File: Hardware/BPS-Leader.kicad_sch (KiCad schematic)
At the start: 28 parts, among them J17 Conn_01x04, J21 SFH11-PBPC-D05-ST-BK, J5 Conn_02x06_Counter_Clockwise, J6 PeripheralCAN, J7 PeripheralCAN, J8 CarCANConnector, Q11 PMV213SN,215, U12 SHT4x

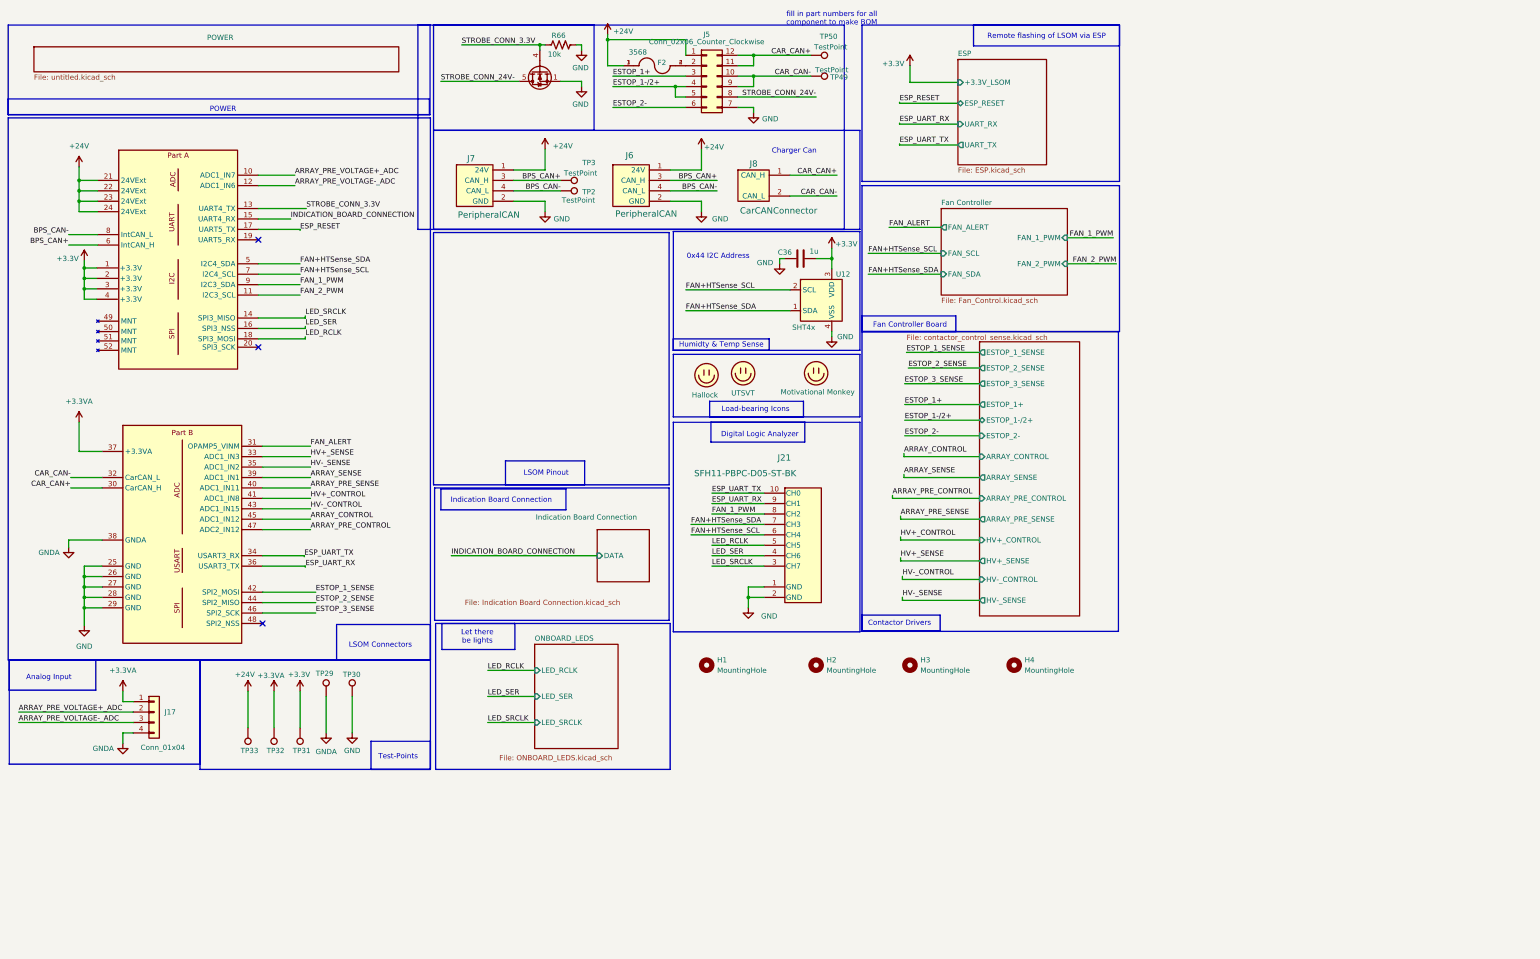
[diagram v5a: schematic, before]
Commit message: RevB PR (#14)
* RevB Schematic Update

* RevB Schematic revisions

* revB updates

* Schematic polishes, layout WIP

* circuit blocks designed, schematic updated

* unblocked SD card holder

* halfway laid-out

* unblocked SD card again

* small schematic changes

* intial layout design

* Updated LSOM footprint

* filled in copper holes. Name/REV/Date added

* RevB layout completed

* JLC Production Files

* added resistors

* replace silkscreen

* condensed custom lirbraries

* removed all unnessasary files and some nessasary ones
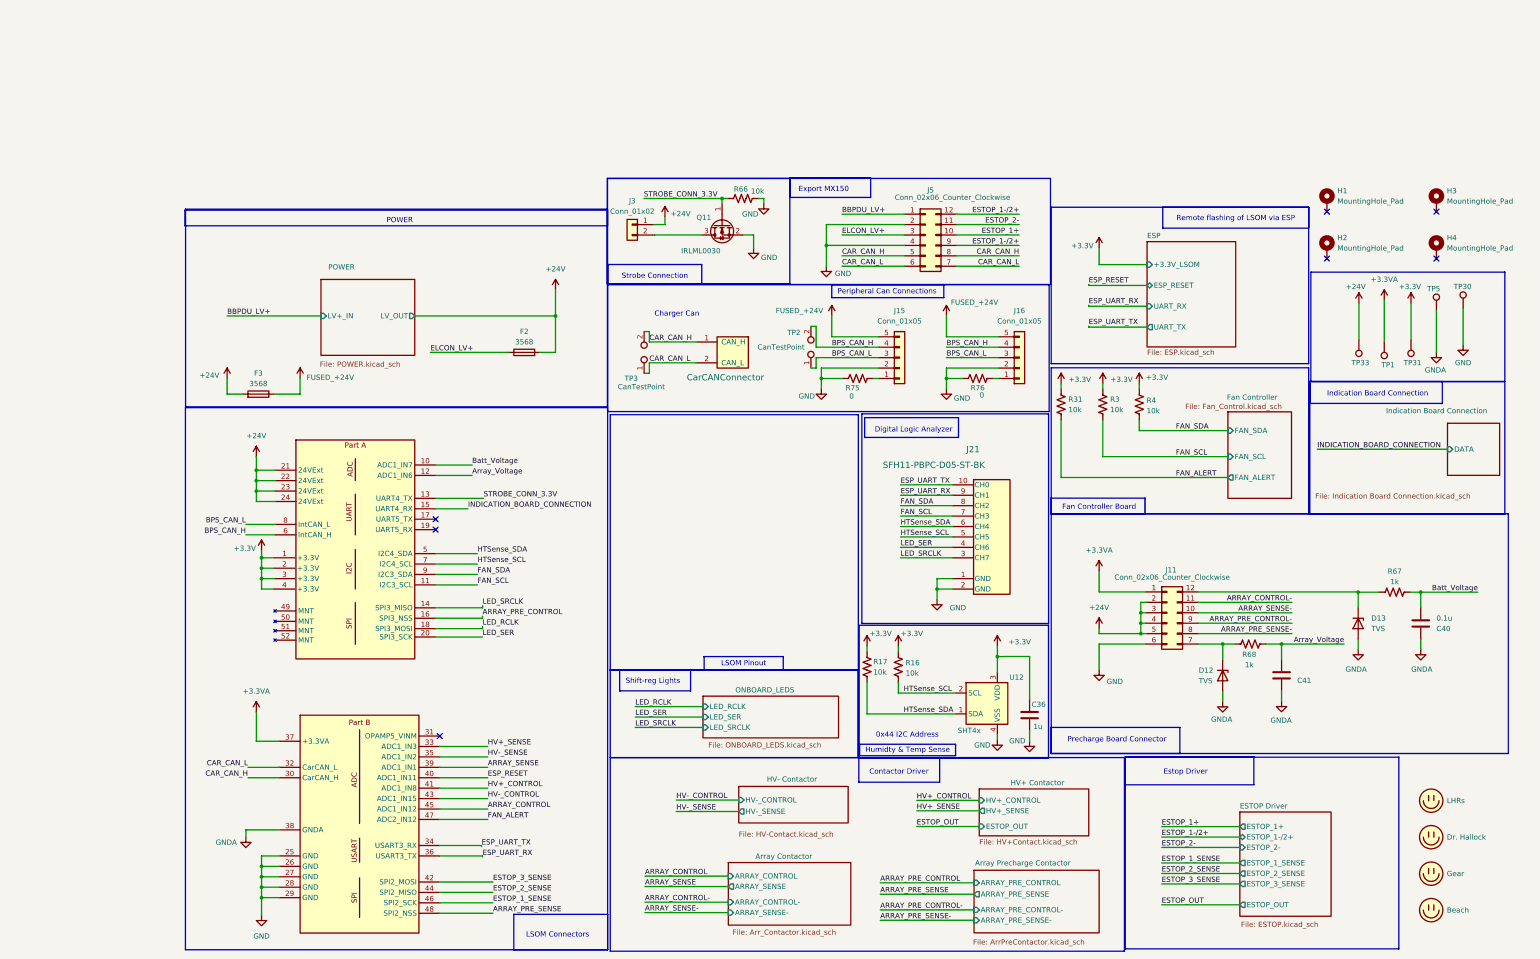
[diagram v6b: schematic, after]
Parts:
- removed F2: 3568, FUSE 3568:3568, symbol 3568:3568
- removed H1, H2, H3, H4: MountingHole, MountingHole:MountingHole_3.2mm_M3, symbol Mechanical:MountingHole
- removed J17: Conn_01x04, UTSVT_Connectors:Molex_Nano-Fit_105309-xx04_1x04_P2.50mm_Vertical, symbol Connector_Generic:Conn_01x04
- removed J6, J7: PeripheralCAN, UTSVT_Connectors:Molex_Nano-Fit_105309-xx04_1x04_P2.50mm_Vertical, symbol utsvt_connectors:PeripheralCANConnector
- removed LOGO1: Motivational Monkey, Custom-KiCadLibraries:Motivational_Monkey2, symbol UTSVT_Misc:Logo_Placeholder
- removed LOGO2: UTSVT, UTSVT_Logos:LHRs_LOGO, symbol UTSVT_Misc:Logo_Placeholder
- removed LOGO3: Hallock, UTSVT_Logos:Hallock_Image_Small, symbol UTSVT_Misc:Logo_Placeholder
- removed Q11: PMV213SN,215, Package_TO_SOT_SMD:SOT-23-3, symbol Transistor_FET:BUK7M27-80EX
- removed TP2, TP29, TP3, TP32, TP49, TP50: TestPoint, TestPoint:TestPoint_Pad_1.0x1.0mm, symbol Connector:TestPoint
- added C40, C41: 0.1u, Capacitor_SMD:C_0603_1608Metric, symbol Device:C
- added D12, D13: TVS, Diode_SMD:D_SOD-123F, symbol Device:D_Zener
- added F2, F3: 3568, CustomKiCad-Library:3568, symbol Device:Fuse
- added H1, H2, H3, H4: MountingHole_Pad, MountingHole:MountingHole_3.2mm_M3_Pad_TopBottom, symbol Mechanical:MountingHole_Pad
- added J11: Conn_02x06_Counter_Clockwise, Connector_Molex:Molex_Nano-Fit_105310-xx12_2x06_P2.50mm_Vertical, symbol Connector_Generic:Conn_02x06_Counter_Clockwise
- added J15, J16: Conn_01x05, Connector_Molex:Molex_Nano-Fit_105309-xx05_1x05_P2.50mm_Vertical, symbol Connector_Generic:Conn_01x05
- added J3: Conn_01x02, Connector_Molex:Molex_Nano-Fit_105313-xx02_1x02_P2.50mm_Horizontal, symbol Connector_Generic:Conn_01x02
- added LOGO1: LHRs, UTSVT_Logos:LHRs_LOGO, symbol utsvt_misc:Logo_Placeholder
- added LOGO2: Dr. Hallock, UTSVT_Logos:Hallock_Image, symbol utsvt_misc:Logo_Placeholder
- added LOGO3: Beach, CustomKiCad-Library:Beach, symbol utsvt_misc:Logo_Placeholder
- added LOGO4: Gear, CustomKiCad-Library:Gear, symbol utsvt_misc:Logo_Placeholder
- added Q11: IRLML0030, Package_TO_SOT_SMD:SOT-23, symbol Transistor_FET:IRLML0030
- added R16, R17, R3, R31, R4: 10k, Resistor_SMD:R_0603_1608Metric, symbol Device:R_US
- added R67, R68: 1k, Resistor_SMD:R_0603_1608Metric, symbol Device:R_US
- added R75, R76: 0, Resistor_SMD:R_0603_1608Metric, symbol Device:R_US
- added TP1: +3.3VA, TestPoint:TestPoint_Keystone_5005-5009_Compact, symbol Connector:TestPoint
- added TP2, TP3: CanTestPoint, Connector_PinHeader_2.54mm:PinHeader_1x02_P2.54mm_Vertical, symbol Connector:TestPoint_2Pole
- added TP5: GNDA, TestPoint:TestPoint_Keystone_5005-5009_Compact, symbol Connector:TestPoint
- C36: LCSC (none) -> C15849
- R66: LCSC (none) -> C25804
- TP30: value TestPoint -> GND; footprint TestPoint:TestPoint_Pad_1.0x1.0mm -> TestPoint:TestPoint_Keystone_5005-5009_Compact
- TP31: value TestPoint -> +3.3V; footprint TestPoint:TestPoint_Pad_1.0x1.0mm -> TestPoint:TestPoint_Keystone_5005-5009_Compact
- TP33: value TestPoint -> +24V; footprint TestPoint:TestPoint_Pad_1.0x1.0mm -> TestPoint:TestPoint_Keystone_5005-5009_Compact
- U12: LCSC (none) -> C5221601
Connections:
- net STROBE_CONN_24V- is gone; now on net CAR_CAN_H: J5.8 (Pin_8)
- net +24V: now also F2.2, F3.2, J11.2 (Pin_2), J11.3 (Pin_3), J11.4 (Pin_4), J11.5 (Pin_5), J3.1 (Pin_1); no longer J5.1 (Pin_1)
- net +3.3V: now also R16.1, R17.1, R3.1, R31.1, R4.1
- net +3.3VA: now also J11.1 (Pin_1), TP1.1
- net ARRAY_PRE_CONTROL: now also J1.16 (SPI3_NSS); no longer J1.47 (ADC2_IN12)
- net ARRAY_PRE_SENSE: now also J1.48 (SPI2_NSS); no longer J1.40 (ADC1_IN11)
- net ESP_RESET: now also J1.40 (ADC1_IN11); no longer J1.17 (UART5_TX)
- net ESTOP_1+: now also J5.10 (Pin_10); no longer J5.3 (Pin_3)
- net ESTOP_1-/2+: now also J5.12 (Pin_12), J5.9 (Pin_9); no longer J5.4 (Pin_4), J5.5 (Pin_5)
- net ESTOP_1_SENSE: now also J1.46 (SPI2_SCK); no longer J1.42 (SPI2_MOSI)
- net ESTOP_2-: now also J5.11 (Pin_11); no longer J5.6 (Pin_6)
- net ESTOP_3_SENSE: now also J1.42 (SPI2_MOSI); no longer J1.46 (SPI2_SCK)
- net FAN_ALERT: now also J1.47 (ADC2_IN12), R31.2; no longer J1.31 (OPAMP5_VINM)
- net GND: now also J5.2 (Pin_2), J5.4 (Pin_4), J11.6 (Pin_6), J15.2 (Pin_2), J16.2 (Pin_2), Q11.2 (S), R75.1, R76.1; no longer J5.7 (Pin_7)
- net GNDA: now also C40.1, C41.1, D12.2 (A), D13.2 (A), TP5.1
- net LED_RCLK: no longer J21.5 (CH5)
- net LED_SER: now also J1.20 (SPI3_SCK); no longer J1.16 (SPI3_NSS)
- net STROBE_CONN_3.3V: now also Q11.1 (G)
- net ARRAY_PRE_VOLTAGE+_ADC renamed Batt_Voltage
- net Batt_Voltage: now also C40.2, R67.1
- net ARRAY_PRE_VOLTAGE-_ADC renamed Array_Voltage
- net Array_Voltage: now also C41.2, R68.1
- net BPS_CAN+ renamed BPS_CAN_H
- net BPS_CAN_H: now also J15.4 (Pin_4), J16.4 (Pin_4), TP2.2
- net BPS_CAN- renamed BPS_CAN_L
- net BPS_CAN_L: now also J15.3 (Pin_3), J16.3 (Pin_3), TP2.1
- net CAR_CAN+ renamed CAR_CAN_H
- net CAR_CAN_H: now also J5.5 (Pin_5), TP3.2; no longer J5.11 (Pin_11), J5.12 (Pin_12)
- net CAR_CAN- renamed CAR_CAN_L
- net CAR_CAN_L: now also J5.6 (Pin_6), J5.7 (Pin_7), TP3.1; no longer J5.10 (Pin_10), J5.9 (Pin_9)
- net FAN+HTSense_SCL renamed HTSense_SCL
- net HTSense_SCL: now also J21.5 (CH5), R16.2; no longer J21.6 (CH4)
- net FAN+HTSense_SDA renamed HTSense_SDA
- net HTSense_SDA: now also J21.6 (CH4), R17.2; no longer J21.7 (CH3)
- net FAN_1_PWM renamed FAN_SDA
- net FAN_SDA: now also R4.2
- net FAN_2_PWM renamed FAN_SCL
- net FAN_SCL: now also J21.7 (CH3), R3.2
- new net: J16.1 (Pin_1), R76.2
- new net: J15.1 (Pin_1), R75.2
- new net: J3.2 (Pin_2), Q11.3 (D)
- new net: D13.1 (K), J11.12 (Pin_12), R67.2
- new net: D12.1 (K), J11.7 (Pin_7), R68.2
- new net ARRAY_CONTROL-: J11.11 (Pin_11)
- new net ARRAY_PRE_CONTROL-: J11.9 (Pin_9)
- new net ARRAY_PRE_SENSE-: J11.8 (Pin_8)
- new net ARRAY_SENSE-: J11.10 (Pin_10)
- new net BBPDU_LV+: J5.1 (Pin_1)
- new net ELCON_LV+: F2.1, J5.3 (Pin_3)
- new net FUSED_+24V: F3.1, J15.5 (Pin_5), J16.5 (Pin_5)
- no-connect marks 3 -> 7
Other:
- removed sheet Contactor Control and Sense
- added sheet Array Contactor (Arr_Contactor.kicad_sch)
- added sheet Array Precharge Contactor (ArrPreContactor.kicad_sch)
- added sheet ESTOP Driver (ESTOP.kicad_sch)
- added sheet HV+ Contactor (HV+Contact.kicad_sch)
- added sheet HV- Contactor (HV-Contact.kicad_sch)
- sheet Fan Controller ports: added none; removed FAN_1_PWM, FAN_2_PWM
- sheet POWER: file untitled.kicad_sch -> POWER.kicad_sch
- sheet POWER ports: added LV+_IN, LV_OUT; removed none
- note added: "Contactor Driver"
- note added: "Estop Driver"
- note added: "Export MX150"
- note added: "Peripheral Can Connections"
- note added: "Precharge Board Connector"
- note added: "Shift-reg Lights"
- note added: "Strobe Connection"
- note removed: "Analog Input"
- note removed: "Contactor Drivers"
- note removed: "Let there be lights"
- note removed: "Load-bearing Icons"
- note removed: "Test-Points"
- note removed: "fill in part numbers for all component to make BOM"
- moved on the sheet: C36, J21, R66, TP30, TP31, TP33, U12
